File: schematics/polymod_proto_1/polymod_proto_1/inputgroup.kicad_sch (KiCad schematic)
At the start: 10 parts

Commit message: pcb layout about to start
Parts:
- J13: renamed from J?; footprint (none) -> Connector_PinSocket_2.54mm:PinSocket_1x08_P2.54mm_Vertical
- R35, R36, R37, R38, R39, R40, R41, R42: renamed from R?; footprint (none) -> Resistor_SMD:R_0805_2012Metric
- U13: renamed from U?; footprint (none) -> Package_SO:SOIC-16_3.9x9.9mm_P1.27mm
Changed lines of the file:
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@@
   (symbol (lib_id "Device:R") (at 118.11 91.44 270)
     (in_bom yes) (on_board yes)
-    (property "Reference" "R?" (id 0) (at 118.11 86.1822 90))
+    (property "Reference" "R40" (id 0) (at 118.11 86.1822 90))
     (property "Value" "10K" (id 1) (at 118.11 88.4936 90))
-    (property "Footprint" "" (id 2) (at 118.11 89.662 90)
+    (property "Footprint" "Resistor_SMD:R_0805_2012Metric" (id 2) (at 118.11 89.662 90)
       (effects (font (size 1.27 1.27)) hide)
     )
@@
   (symbol (lib_id "74xx:74LS165") (at 175.26 90.17 0)
     (in_bom yes) (on_board yes)
-    (property "Reference" "U?" (id 0) (at 182.88 64.77 0))
+    (property "Reference" "U13" (id 0) (at 182.88 64.77 0))
     (property "Value" "74LS165" (id 1) (at 182.88 67.31 0))
-    (property "Footprint" "" (id 2) (at 175.26 90.17 0)
+    (property "Footprint" "Package_SO:SOIC-16_3.9x9.9mm_P1.27mm" (id 2) (at 175.26 90.17 0)
       (effects (font (size 1.27 1.27)) hide)
     )
@@
   (symbol (lib_id "Connector:Conn_01x08_Male") (at 133.35 85.09 0)
     (in_bom yes) (on_board yes)
-    (property "Reference" "J?" (id 0) (at 136.0932 72.8726 0))
+    (property "Reference" "J13" (id 0) (at 136.0932 72.8726 0))
     (property "Value" "Conn_01x08_Male" (id 1) (at 137.16 74.93 0))
-    (property "Footprint" "" (id 2) (at 133.35 85.09 0)
+    (property "Footprint" "Connector_PinSocket_2.54mm:PinSocket_1x08_P2.54mm_Vertical" (id 2) (at 133.35 85.09 0)
       (effects (font (size 1.27 1.27)) hide)
     )
@@
   (symbol (lib_id "power:VCC") (at 175.26 67.31 0)
     (in_bom yes) (on_board yes)
-    (property "Reference" "#PWR?" (id 0) (at 175.26 71.12 0)
+    (property "Reference" "#PWR030" (id 0) (at 175.26 71.12 0)
       (effects (font (size 1.27 1.27)) hide)
     )
@@
   (symbol (lib_id "Device:R") (at 102.87 96.52 270)
     (in_bom yes) (on_board yes)
-    (property "Reference" "R?" (id 0) (at 102.87 91.2622 90))
+    (property "Reference" "R36" (id 0) (at 102.87 91.2622 90))
     (property "Value" "10K" (id 1) (at 102.87 93.5736 90))
-    (property "Footprint" "" (id 2) (at 102.87 94.742 90)
+    (property "Footprint" "Resistor_SMD:R_0805_2012Metric" (id 2) (at 102.87 94.742 90)
       (effects (font (size 1.27 1.27)) hide)
     )
@@
   (symbol (lib_id "Device:R") (at 102.87 86.36 270)
     (in_bom yes) (on_board yes)
-    (property "Reference" "R?" (id 0) (at 102.87 81.1022 90))
+    (property "Reference" "R35" (id 0) (at 102.87 81.1022 90))
     (property "Value" "10K" (id 1) (at 102.87 83.4136 90))
-    (property "Footprint" "" (id 2) (at 102.87 84.582 90)
+    (property "Footprint" "Resistor_SMD:R_0805_2012Metric" (id 2) (at 102.87 84.582 90)
       (effects (font (size 1.27 1.27)) hide)
     )
@@
   (symbol (lib_id "Device:R") (at 118.11 81.28 270)
     (in_bom yes) (on_board yes)
-    (property "Reference" "R?" (id 0) (at 118.11 76.0222 90))
+    (property "Reference" "R39" (id 0) (at 118.11 76.0222 90))
     (property "Value" "10K" (id 1) (at 118.11 78.3336 90))
-    (property "Footprint" "" (id 2) (at 118.11 79.502 90)
+    (property "Footprint" "Resistor_SMD:R_0805_2012Metric" (id 2) (at 118.11 79.502 90)
       (effects (font (size 1.27 1.27)) hide)
     )
@@
   (symbol (lib_id "Device:R") (at 110.49 83.82 270)
     (in_bom yes) (on_board yes)
-    (property "Reference" "R?" (id 0) (at 110.49 78.5622 90))
+    (property "Reference" "R37" (id 0) (at 110.49 78.5622 90))
     (property "Value" "10K" (id 1) (at 110.49 80.8736 90))
-    (property "Footprint" "" (id 2) (at 110.49 82.042 90)
+    (property "Footprint" "Resistor_SMD:R_0805_2012Metric" (id 2) (at 110.49 82.042 90)
       (effects (font (size 1.27 1.27)) hide)
     )
@@
   (symbol (lib_id "Device:R") (at 125.73 88.9 270)
     (in_bom yes) (on_board yes)
-    (property "Reference" "R?" (id 0) (at 125.73 83.6422 90))
+    (property "Reference" "R42" (id 0) (at 125.73 83.6422 90))
     (property "Value" "10K" (id 1) (at 125.73 85.9536 90))
-    (property "Footprint" "" (id 2) (at 125.73 87.122 90)
+    (property "Footprint" "Resistor_SMD:R_0805_2012Metric" (id 2) (at 125.73 87.122 90)
       (effects (font (size 1.27 1.27)) hide)
     )
@@
   (symbol (lib_id "Device:R") (at 125.73 78.74 270)
     (in_bom yes) (on_board yes)
-    (property "Reference" "R?" (id 0) (at 125.73 73.4822 90))
+    (property "Reference" "R41" (id 0) (at 125.73 73.4822 90))
     (property "Value" "10K" (id 1) (at 125.73 75.7936 90))
-    (property "Footprint" "" (id 2) (at 125.73 76.962 90)
+    (property "Footprint" "Resistor_SMD:R_0805_2012Metric" (id 2) (at 125.73 76.962 90)
       (effects (font (size 1.27 1.27)) hide)
     )
@@
   (symbol (lib_id "power:GND") (at 175.26 115.57 0)
     (in_bom yes) (on_board yes)
-    (property "Reference" "#PWR?" (id 0) (at 175.26 121.92 0)
+    (property "Reference" "#PWR031" (id 0) (at 175.26 121.92 0)
       (effects (font (size 1.27 1.27)) hide)
     )
@@
   (symbol (lib_id "Device:R") (at 110.49 93.98 270)
     (in_bom yes) (on_board yes)
-    (property "Reference" "R?" (id 0) (at 110.49 88.7222 90))
+    (property "Reference" "R38" (id 0) (at 110.49 88.7222 90))
     (property "Value" "10K" (id 1) (at 110.49 91.0336 90))
-    (property "Footprint" "" (id 2) (at 110.49 92.202 90)
+    (property "Footprint" "Resistor_SMD:R_0805_2012Metric" (id 2) (at 110.49 92.202 90)
       (effects (font (size 1.27 1.27)) hide)
     )

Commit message: routing started
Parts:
- renumbered J13 to J11, R35 to R19, R36 to R20, R37 to R21, R38 to R22, R39 to R23, R40 to R24, R41 to R25, R42 to R26, U13 to U11
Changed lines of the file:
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@@
   (symbol (lib_id "Device:R") (at 118.11 91.44 270)
     (in_bom yes) (on_board yes)
-    (property "Reference" "R40" (id 0) (at 118.11 86.1822 90))
+    (property "Reference" "R24" (id 0) (at 118.11 86.1822 90))
     (property "Value" "10K" (id 1) (at 118.11 88.4936 90))
     (property "Footprint" "Resistor_SMD:R_0805_2012Metric" (id 2) (at 118.11 89.662 90)
@@
   (symbol (lib_id "74xx:74LS165") (at 175.26 90.17 0)
     (in_bom yes) (on_board yes)
-    (property "Reference" "U13" (id 0) (at 182.88 64.77 0))
+    (property "Reference" "U11" (id 0) (at 182.88 64.77 0))
     (property "Value" "74LS165" (id 1) (at 182.88 67.31 0))
     (property "Footprint" "Package_SO:SOIC-16_3.9x9.9mm_P1.27mm" (id 2) (at 175.26 90.17 0)
@@
   (symbol (lib_id "Connector:Conn_01x08_Male") (at 133.35 85.09 0)
     (in_bom yes) (on_board yes)
-    (property "Reference" "J13" (id 0) (at 136.0932 72.8726 0))
+    (property "Reference" "J11" (id 0) (at 136.0932 72.8726 0))
     (property "Value" "Conn_01x08_Male" (id 1) (at 137.16 74.93 0))
     (property "Footprint" "Connector_PinSocket_2.54mm:PinSocket_1x08_P2.54mm_Vertical" (id 2) (at 133.35 85.09 0)
@@
   (symbol (lib_id "power:VCC") (at 175.26 67.31 0)
     (in_bom yes) (on_board yes)
-    (property "Reference" "#PWR030" (id 0) (at 175.26 71.12 0)
+    (property "Reference" "#PWR026" (id 0) (at 175.26 71.12 0)
       (effects (font (size 1.27 1.27)) hide)
     )
@@
   (symbol (lib_id "Device:R") (at 102.87 96.52 270)
     (in_bom yes) (on_board yes)
-    (property "Reference" "R36" (id 0) (at 102.87 91.2622 90))
+    (property "Reference" "R20" (id 0) (at 102.87 91.2622 90))
     (property "Value" "10K" (id 1) (at 102.87 93.5736 90))
     (property "Footprint" "Resistor_SMD:R_0805_2012Metric" (id 2) (at 102.87 94.742 90)
@@
   (symbol (lib_id "Device:R") (at 102.87 86.36 270)
     (in_bom yes) (on_board yes)
-    (property "Reference" "R35" (id 0) (at 102.87 81.1022 90))
+    (property "Reference" "R19" (id 0) (at 102.87 81.1022 90))
     (property "Value" "10K" (id 1) (at 102.87 83.4136 90))
     (property "Footprint" "Resistor_SMD:R_0805_2012Metric" (id 2) (at 102.87 84.582 90)
@@
   (symbol (lib_id "Device:R") (at 118.11 81.28 270)
     (in_bom yes) (on_board yes)
-    (property "Reference" "R39" (id 0) (at 118.11 76.0222 90))
+    (property "Reference" "R23" (id 0) (at 118.11 76.0222 90))
     (property "Value" "10K" (id 1) (at 118.11 78.3336 90))
     (property "Footprint" "Resistor_SMD:R_0805_2012Metric" (id 2) (at 118.11 79.502 90)
@@
   (symbol (lib_id "Device:R") (at 110.49 83.82 270)
     (in_bom yes) (on_board yes)
-    (property "Reference" "R37" (id 0) (at 110.49 78.5622 90))
+    (property "Reference" "R21" (id 0) (at 110.49 78.5622 90))
     (property "Value" "10K" (id 1) (at 110.49 80.8736 90))
     (property "Footprint" "Resistor_SMD:R_0805_2012Metric" (id 2) (at 110.49 82.042 90)
@@
   (symbol (lib_id "Device:R") (at 125.73 88.9 270)
     (in_bom yes) (on_board yes)
-    (property "Reference" "R42" (id 0) (at 125.73 83.6422 90))
+    (property "Reference" "R26" (id 0) (at 125.73 83.6422 90))
     (property "Value" "10K" (id 1) (at 125.73 85.9536 90))
     (property "Footprint" "Resistor_SMD:R_0805_2012Metric" (id 2) (at 125.73 87.122 90)
@@
   (symbol (lib_id "Device:R") (at 125.73 78.74 270)
     (in_bom yes) (on_board yes)
-    (property "Reference" "R41" (id 0) (at 125.73 73.4822 90))
+    (property "Reference" "R25" (id 0) (at 125.73 73.4822 90))
     (property "Value" "10K" (id 1) (at 125.73 75.7936 90))
     (property "Footprint" "Resistor_SMD:R_0805_2012Metric" (id 2) (at 125.73 76.962 90)
@@
   (symbol (lib_id "power:GND") (at 175.26 115.57 0)
     (in_bom yes) (on_board yes)
-    (property "Reference" "#PWR031" (id 0) (at 175.26 121.92 0)
+    (property "Reference" "#PWR027" (id 0) (at 175.26 121.92 0)
       (effects (font (size 1.27 1.27)) hide)
     )
@@
   (symbol (lib_id "Device:R") (at 110.49 93.98 270)
     (in_bom yes) (on_board yes)
-    (property "Reference" "R38" (id 0) (at 110.49 88.7222 90))
+    (property "Reference" "R22" (id 0) (at 110.49 88.7222 90))
     (property "Value" "10K" (id 1) (at 110.49 91.0336 90))
     (property "Footprint" "Resistor_SMD:R_0805_2012Metric" (id 2) (at 110.49 92.202 90)

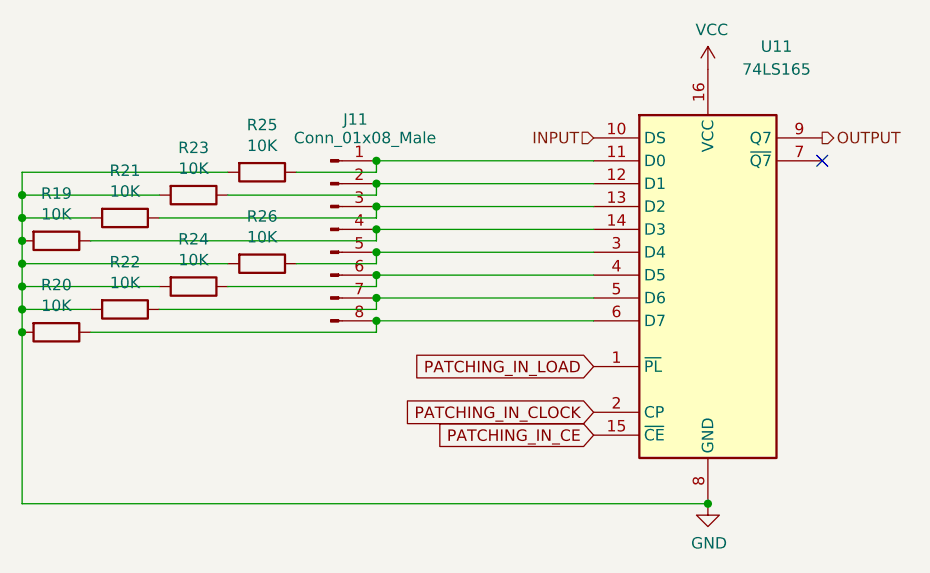
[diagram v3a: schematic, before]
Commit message: better layout/routing
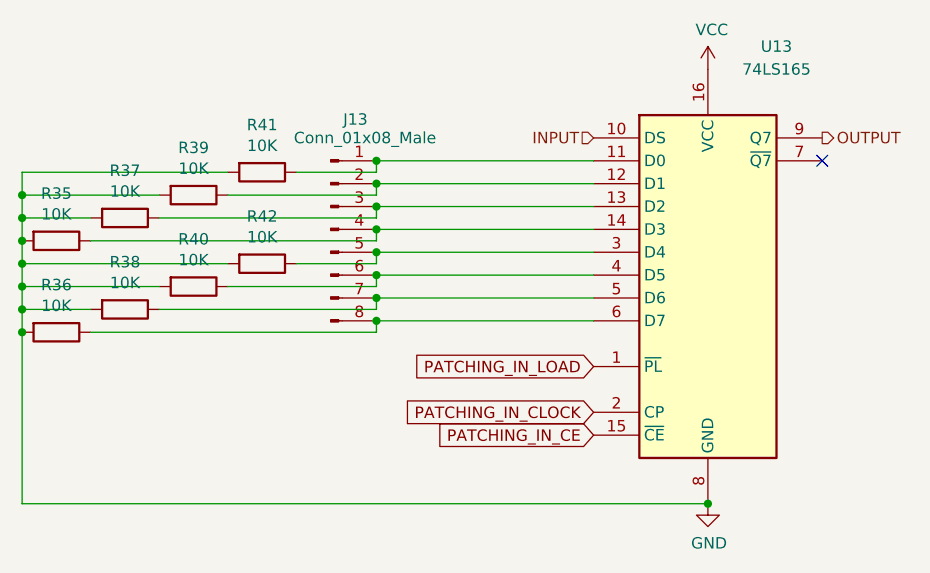
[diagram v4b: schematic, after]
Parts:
- renumbered J11 to J13, R19 to R35, R20 to R36, R21 to R37, R22 to R38, R23 to R39, R24 to R40, R25 to R41, R26 to R42, U11 to U13
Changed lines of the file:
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@@
   (symbol (lib_id "Device:R") (at 118.11 91.44 270)
     (in_bom yes) (on_board yes)
-    (property "Reference" "R24" (id 0) (at 118.11 86.1822 90))
+    (property "Reference" "R40" (id 0) (at 118.11 86.1822 90))
     (property "Value" "10K" (id 1) (at 118.11 88.4936 90))
     (property "Footprint" "Resistor_SMD:R_0805_2012Metric" (id 2) (at 118.11 89.662 90)
@@
   (symbol (lib_id "74xx:74LS165") (at 175.26 90.17 0)
     (in_bom yes) (on_board yes)
-    (property "Reference" "U11" (id 0) (at 182.88 64.77 0))
+    (property "Reference" "U13" (id 0) (at 182.88 64.77 0))
     (property "Value" "74LS165" (id 1) (at 182.88 67.31 0))
     (property "Footprint" "Package_SO:SOIC-16_3.9x9.9mm_P1.27mm" (id 2) (at 175.26 90.17 0)
@@
   (symbol (lib_id "Connector:Conn_01x08_Male") (at 133.35 85.09 0)
     (in_bom yes) (on_board yes)
-    (property "Reference" "J11" (id 0) (at 136.0932 72.8726 0))
+    (property "Reference" "J13" (id 0) (at 136.0932 72.8726 0))
     (property "Value" "Conn_01x08_Male" (id 1) (at 137.16 74.93 0))
     (property "Footprint" "Connector_PinSocket_2.54mm:PinSocket_1x08_P2.54mm_Vertical" (id 2) (at 133.35 85.09 0)
@@
   (symbol (lib_id "Device:R") (at 102.87 96.52 270)
     (in_bom yes) (on_board yes)
-    (property "Reference" "R20" (id 0) (at 102.87 91.2622 90))
+    (property "Reference" "R36" (id 0) (at 102.87 91.2622 90))
     (property "Value" "10K" (id 1) (at 102.87 93.5736 90))
     (property "Footprint" "Resistor_SMD:R_0805_2012Metric" (id 2) (at 102.87 94.742 90)
@@
   (symbol (lib_id "Device:R") (at 102.87 86.36 270)
     (in_bom yes) (on_board yes)
-    (property "Reference" "R19" (id 0) (at 102.87 81.1022 90))
+    (property "Reference" "R35" (id 0) (at 102.87 81.1022 90))
     (property "Value" "10K" (id 1) (at 102.87 83.4136 90))
     (property "Footprint" "Resistor_SMD:R_0805_2012Metric" (id 2) (at 102.87 84.582 90)
@@
   (symbol (lib_id "Device:R") (at 118.11 81.28 270)
     (in_bom yes) (on_board yes)
-    (property "Reference" "R23" (id 0) (at 118.11 76.0222 90))
+    (property "Reference" "R39" (id 0) (at 118.11 76.0222 90))
     (property "Value" "10K" (id 1) (at 118.11 78.3336 90))
     (property "Footprint" "Resistor_SMD:R_0805_2012Metric" (id 2) (at 118.11 79.502 90)
@@
   (symbol (lib_id "Device:R") (at 110.49 83.82 270)
     (in_bom yes) (on_board yes)
-    (property "Reference" "R21" (id 0) (at 110.49 78.5622 90))
+    (property "Reference" "R37" (id 0) (at 110.49 78.5622 90))
     (property "Value" "10K" (id 1) (at 110.49 80.8736 90))
     (property "Footprint" "Resistor_SMD:R_0805_2012Metric" (id 2) (at 110.49 82.042 90)
@@
   (symbol (lib_id "Device:R") (at 125.73 88.9 270)
     (in_bom yes) (on_board yes)
-    (property "Reference" "R26" (id 0) (at 125.73 83.6422 90))
+    (property "Reference" "R42" (id 0) (at 125.73 83.6422 90))
     (property "Value" "10K" (id 1) (at 125.73 85.9536 90))
     (property "Footprint" "Resistor_SMD:R_0805_2012Metric" (id 2) (at 125.73 87.122 90)
@@
   (symbol (lib_id "Device:R") (at 125.73 78.74 270)
     (in_bom yes) (on_board yes)
-    (property "Reference" "R25" (id 0) (at 125.73 73.4822 90))
+    (property "Reference" "R41" (id 0) (at 125.73 73.4822 90))
     (property "Value" "10K" (id 1) (at 125.73 75.7936 90))
     (property "Footprint" "Resistor_SMD:R_0805_2012Metric" (id 2) (at 125.73 76.962 90)
@@
   (symbol (lib_id "Device:R") (at 110.49 93.98 270)
     (in_bom yes) (on_board yes)
-    (property "Reference" "R22" (id 0) (at 110.49 88.7222 90))
+    (property "Reference" "R38" (id 0) (at 110.49 88.7222 90))
     (property "Value" "10K" (id 1) (at 110.49 91.0336 90))
     (property "Footprint" "Resistor_SMD:R_0805_2012Metric" (id 2) (at 110.49 92.202 90)
